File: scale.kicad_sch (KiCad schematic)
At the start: 10 parts, among them J1 Conn_01x02_Pin, J2 Conn_01x04_Pin, J4 Conn_01x05_Pin

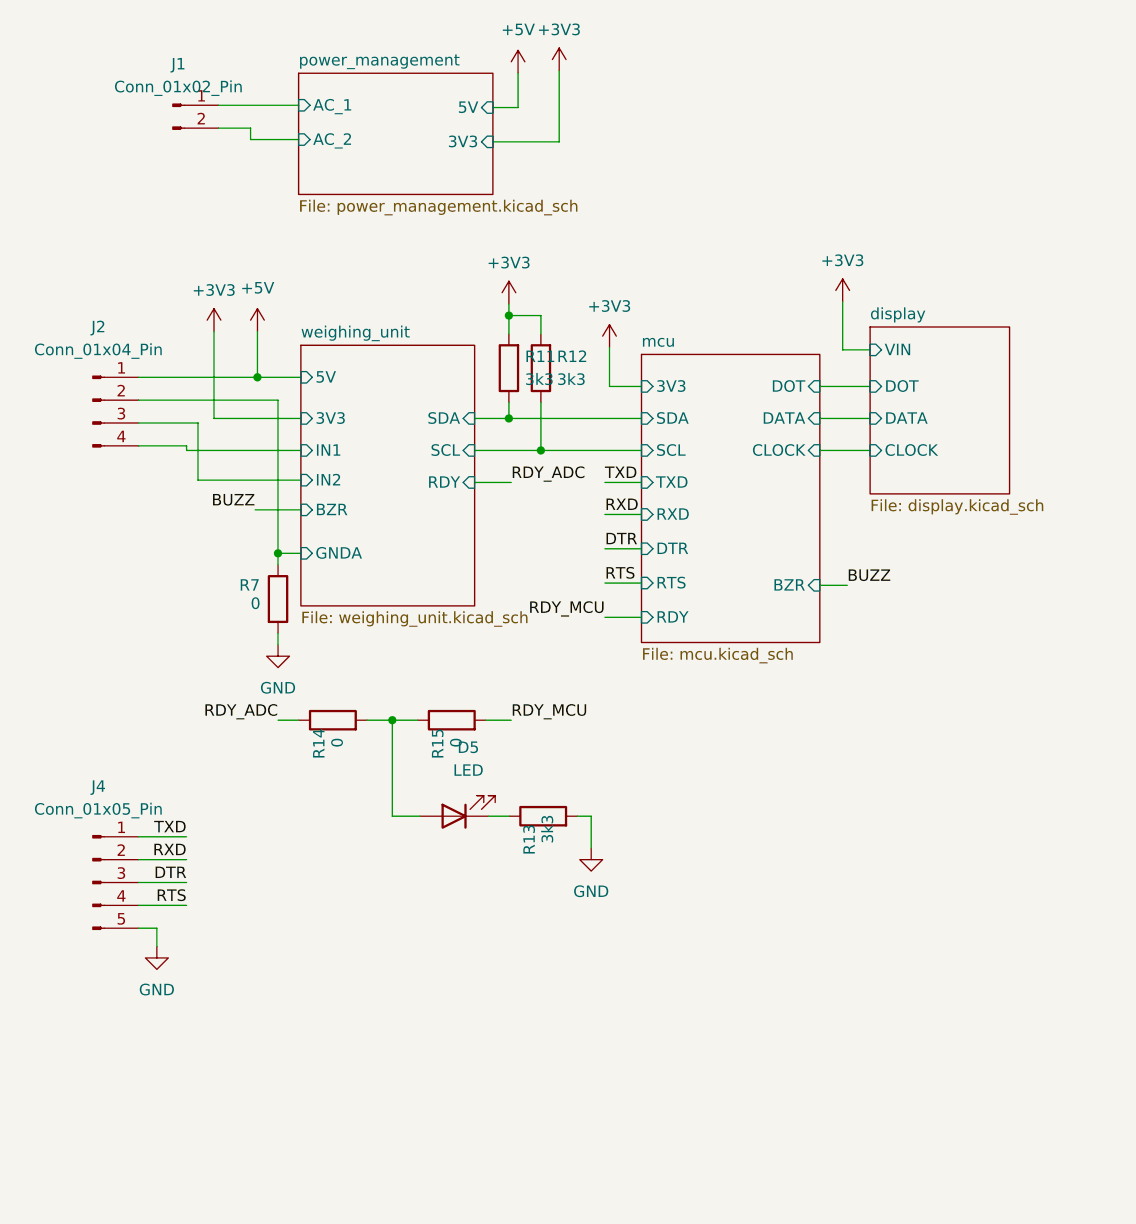
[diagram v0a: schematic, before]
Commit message: change dimensions
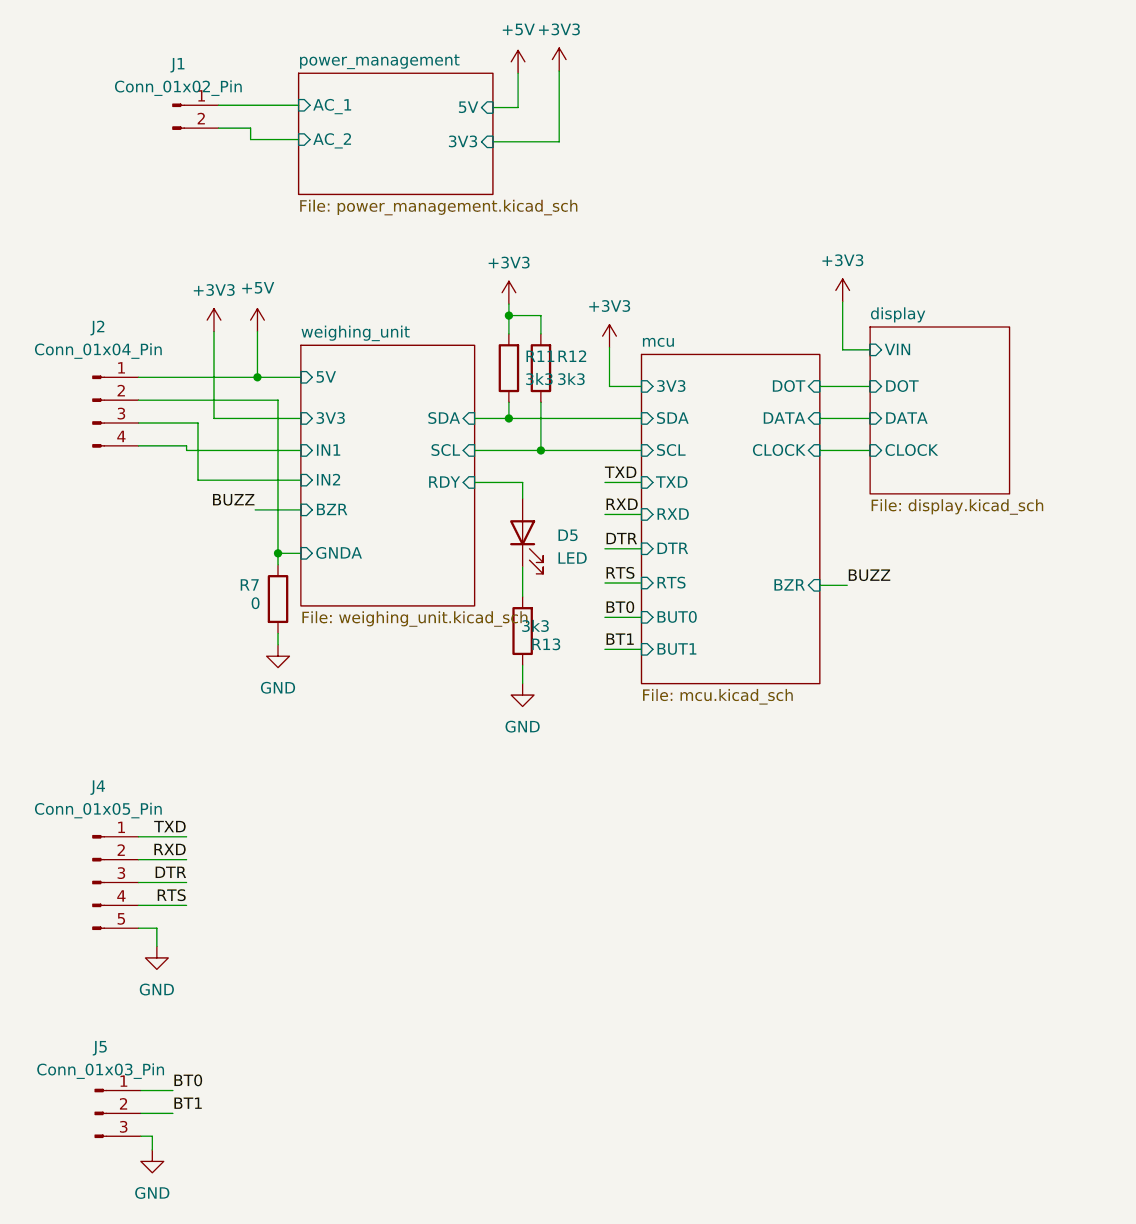
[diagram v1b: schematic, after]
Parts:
- removed R14, R15: 0, Resistor_SMD:R_0402_1005Metric, symbol Device:R
- added J5: Conn_01x03_Pin, BBG:CONN_S3B-XH-ALFSN_JST, symbol Connector:Conn_01x03_Pin
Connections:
- net GND: now also R13.1, J5.3 (Pin_3); no longer R13.2
- net weighing_unit/RDY: now reaches D5.2 (A)
- net at D5.1 (K): now also R13.2; no longer R13.1
- new net BT0: J5.1 (Pin_1)
- new net BT1: J5.2 (Pin_2)
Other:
- sheet mcu ports: added BUT0, BUT1; removed RDY
- moved on the sheet: D5, R13
